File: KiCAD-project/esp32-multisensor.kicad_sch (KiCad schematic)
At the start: 21 parts, among them J1 USB_C_Receptacle_USB2.0, SW1 RST, SW3 BOOT, U1 ESP32-WROOM-E, U2 AMS1117-3.3, U3 TPD4E02B04DQA

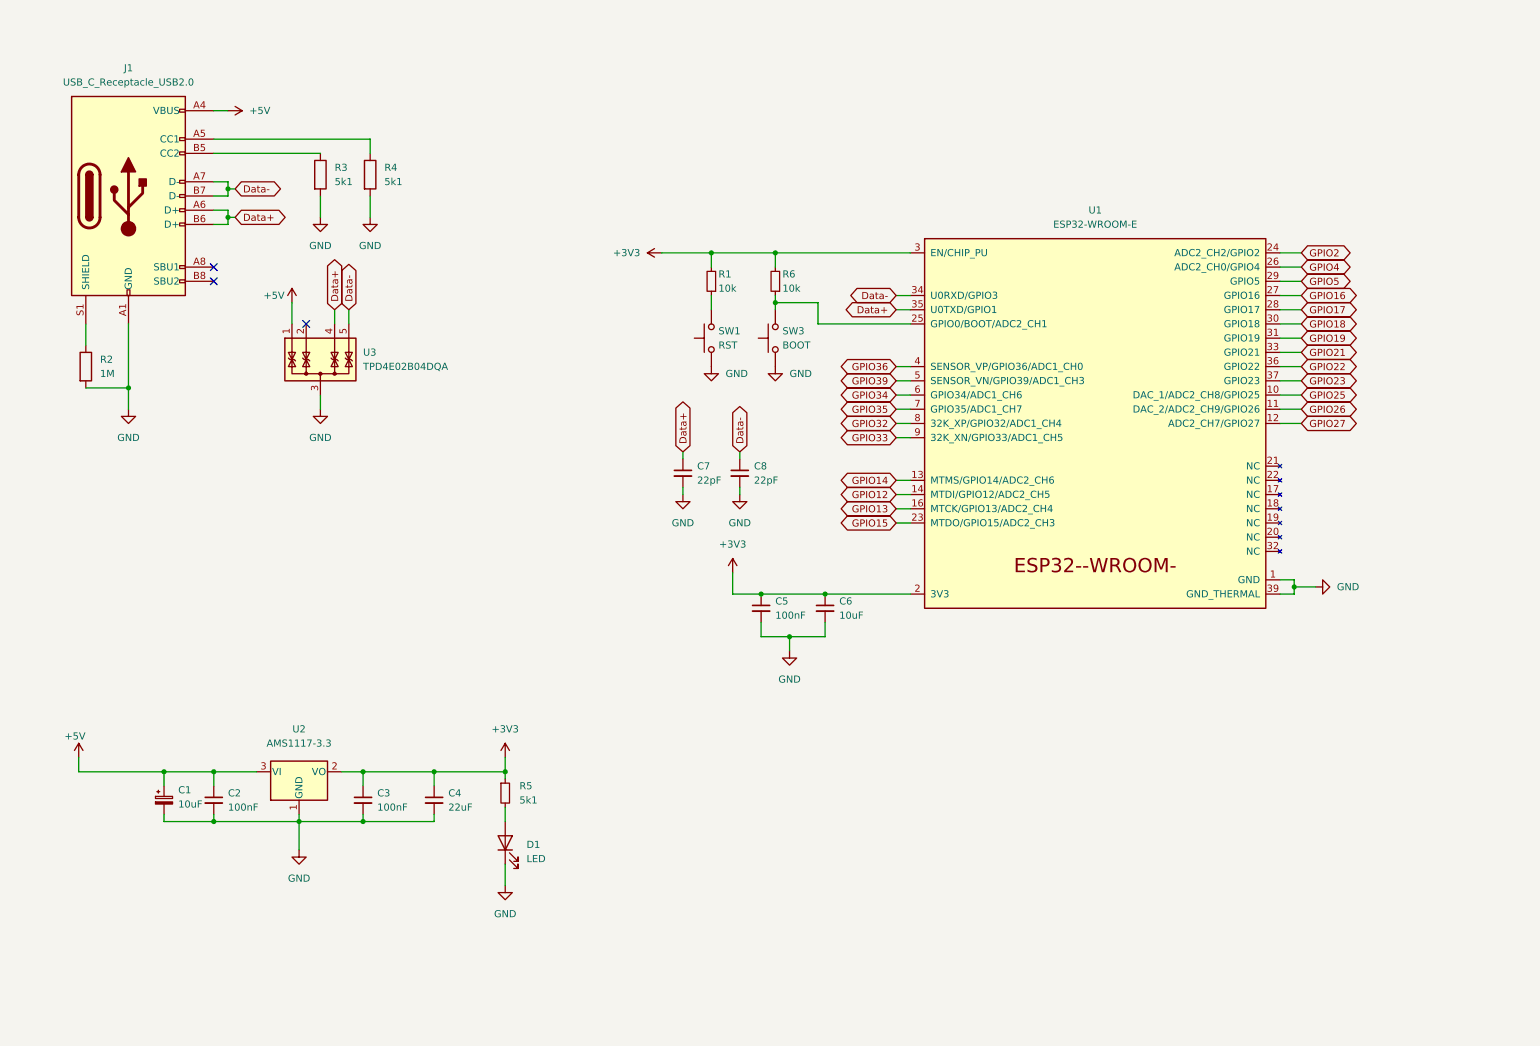
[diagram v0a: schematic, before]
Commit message: schematic created + base pcb
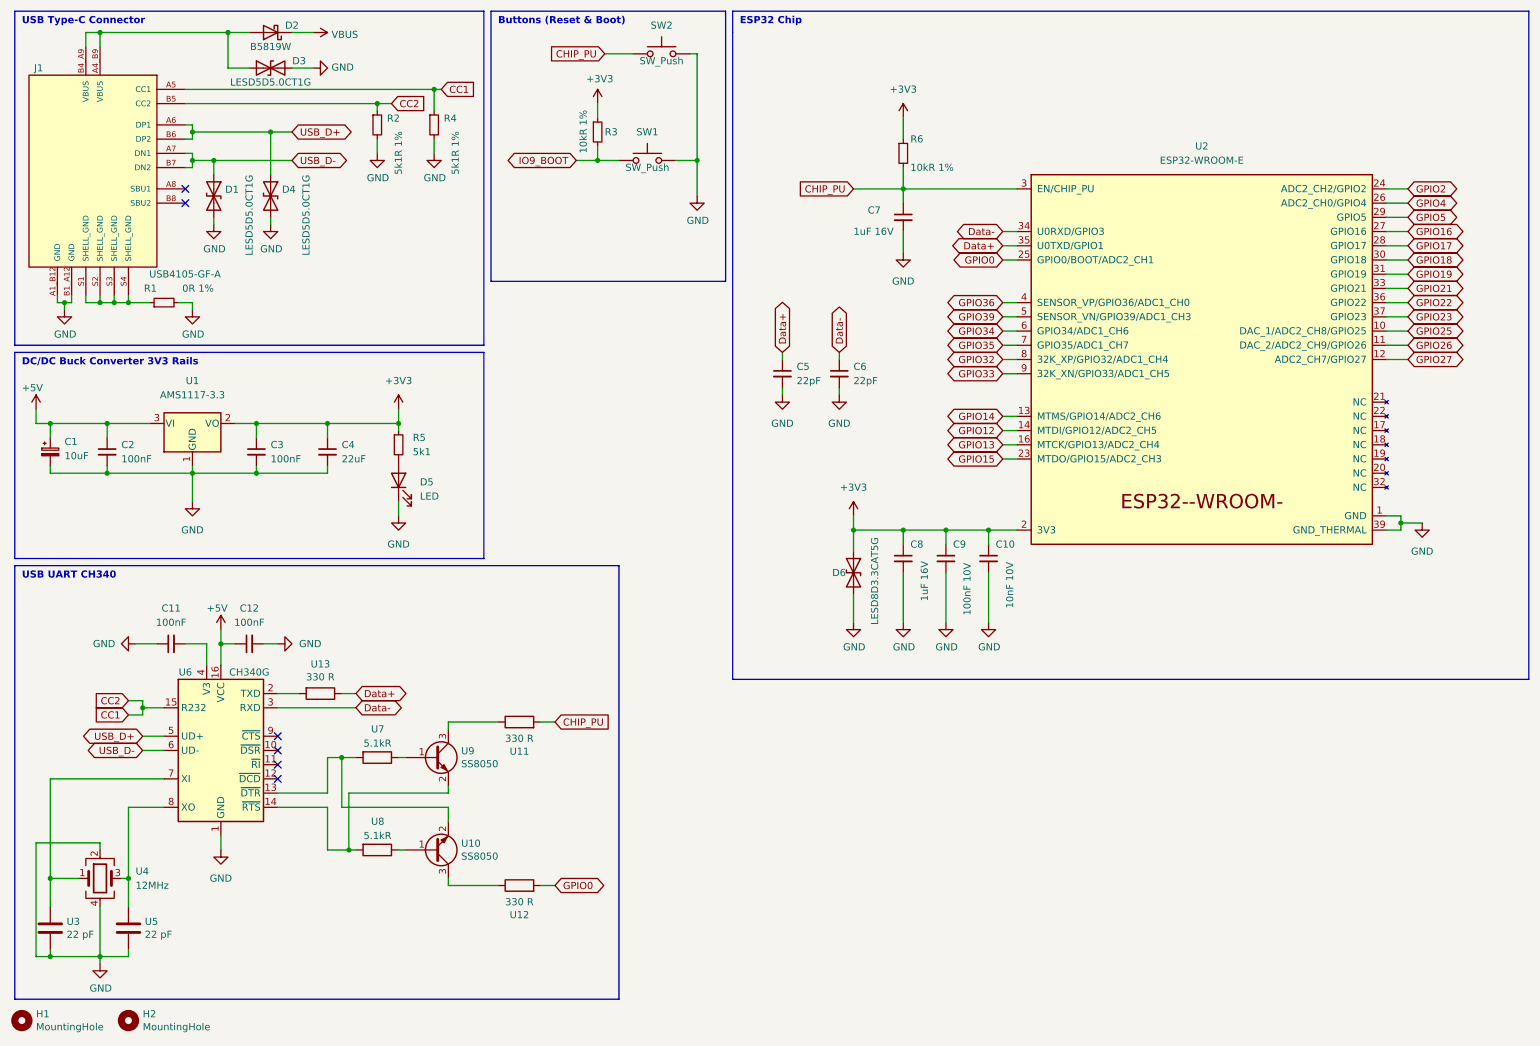
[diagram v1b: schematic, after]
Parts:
- removed C5: 100nF, symbol Device:C_Small
- removed C6: 10uF, symbol Device:C_Small
- removed J1: USB_C_Receptacle_USB2.0, Connector_USB:USB_C_Receptacle_HRO_TYPE-C-31-M-12, symbol Connector:USB_C_Receptacle_USB2.0
- removed R2: 1M, Resistor_SMD:R_0805_2012Metric_Pad1.20x1.40mm_HandSolder, symbol Device:R
- removed R3, R4: 5k1, Resistor_SMD:R_0805_2012Metric_Pad1.20x1.40mm_HandSolder, symbol Device:R
- removed SW3: BOOT, Button_Switch_SMD:SW_Push_1P1T_NO_CK_KMR2, symbol Switch:SW_Push
- removed U3: TPD4E02B04DQA, Package_SON:USON-10_2.5x1.0mm_P0.5mm, symbol Power_Protection:TPD4E02B04DQA
- added C10: 10nF 10V, Capacitor_THT:CP_Radial_D5.0mm_P2.50mm, symbol Device:C_Small
- added C11, C12: 100nF, Capacitor_THT:CP_Radial_D5.0mm_P2.50mm, symbol Device:C_Small
- added C7, C8: 1uF 16V, Capacitor_THT:CP_Radial_D5.0mm_P2.50mm, symbol Device:C_Small
- added C9: 100nF 10V, Capacitor_THT:CP_Radial_D5.0mm_P2.50mm, symbol Device:C_Small
- added D1, D4: LESD5D5.0CT1G, Diode_SMD:D_SOD-123, symbol Device:D_TVS
- added D2: B5819W, Diode_THT:D_A-405_P10.16mm_Horizontal, symbol Device:D_Schottky
- added D3: LESD5D5.0CT1G, Diode_SMD:D_SOD-923, symbol Device:D_TVS
- added D6: LESD8D3.3CAT5G, Rust_Board:SOD-882, symbol Device:D_TVS
- added H1, H2: MountingHole, ToolingHole:ToolingHole_JLCSMT, symbol Mechanical:MountingHole
- added J1: USB4105-GF-A, esp32_multisensor:GCT_USB4105-GF-A, symbol Rust_Board:USB4105-GF-A
- added R2, R4: 5k1R 1%, Resistor_THT:R_Axial_DIN0207_L6.3mm_D2.5mm_P10.16mm_Horizontal, symbol Device:R_Small
- added R3: 10kR 1%, Resistor_THT:R_Axial_DIN0207_L6.3mm_D2.5mm_P10.16mm_Horizontal, symbol Device:R_Small
- added SW2: SW_Push, esp32_multisensor:SW_147873-2, symbol Switch:SW_Push
- added U10, U9: SS8050, Package_TO_SOT_SMD:SOT-23, symbol Transistor_BJT:MMBT3904
- added U11, U12, U13: 330 R, Resistor_SMD:R_0402_1005Metric, symbol Device:R
- added U3, U5: 22 pF, Capacitor_SMD:C_0402_1005Metric, symbol Device:C
- added U4: 12MHz, Crystal:Crystal_SMD_3225-4Pin_3.2x2.5mm, symbol Device:Crystal_GND24
- added U6: CH340G, Package_SO:SOIC-16_3.9x9.9mm_P1.27mm, symbol Interface_USB:CH340G
- added U7, U8: 5.1kR, Resistor_SMD:R_0402_1005Metric, symbol Device:R
- C1: footprint (none) -> Capacitor_THT:CP_Radial_Tantal_D4.5mm_P2.50mm
- C2, C3, C4: footprint (none) -> Capacitor_THT:CP_Radial_D5.0mm_P2.50mm
- C5: renamed from C7; footprint (none) -> Capacitor_THT:CP_Radial_D5.0mm_P2.50mm
- C6: renamed from C8; footprint (none) -> Capacitor_THT:CP_Radial_D5.0mm_P2.50mm
- D5: renamed from D1; footprint (none) -> LED_SMD:LED_0805_2012Metric_Pad1.15x1.40mm_HandSolder
- R1: value 10k -> 0R 1%; footprint Resistor_SMD:R_0805_2012Metric_Pad1.20x1.40mm_HandSolder -> Resistor_THT:R_Axial_DIN0207_L6.3mm_D2.5mm_P10.16mm_Horizontal; FARNELL (none) -> 2329957
- R5: footprint Resistor_SMD:R_0805_2012Metric_Pad1.20x1.40mm_HandSolder -> Resistor_THT:R_Axial_DIN0207_L6.3mm_D2.5mm_P10.16mm_Horizontal
- R6: value 10k -> 10kR 1%; footprint Resistor_SMD:R_0805_2012Metric_Pad1.20x1.40mm_HandSolder -> Resistor_THT:R_Axial_DIN0207_L6.3mm_D2.5mm_P10.16mm_Horizontal; FARNELL (none) -> 2329855
- SW1: value RST -> SW_Push; footprint Button_Switch_SMD:SW_Push_1P1T_NO_CK_KMR2 -> esp32_multisensor:SW_147873-2; LCSC (none) -> C116501
- renumbered U2 to U1, U1 to U2
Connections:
- net +3V3: now also R6.1, C10.1, C8.1, C9.1, D6.1 (A1), R3.1; no longer R1.2, R6.2, U2.3 (EN/CHIP_PU)
- net +5V: now also C12.1, U6.16 (VCC)
- net Data+: now also U13.1
- net Data-: now also U6.3 (RXD)
- net GND: now also R1.2, SW1.2, C10.2, C11.1, C12.2, C7.2, C8.2, C9.2, D1.2 (A2), D3.2 (A2), D4.2 (A2), D6.2 (A2), J1.A1_B12 (GND), J1.B1_A12 (GND), R2.2, R4.2, SW2.2, U3.2, U4.2, U4.4, U5.2, U6.1 (GND); no longer SW1.1
- net GPIO0: now reaches U2.25 (GPIO0/BOOT/ADC2_CH1)
- net GPIO0: now also U12.2; no longer R6.1
- net at R1.1: now also J1.S1 (SHELL_GND), J1.S2 (SHELL_GND), J1.S3 (SHELL_GND), J1.S4 (SHELL_GND); no longer SW1.2
- new net: U11.1, U9.3 (C)
- new net: U13.2, U6.2 (TXD)
- new net: D2.2 (A), D3.1 (A1), J1.A4_B9 (VBUS), J1.B4_A9 (VBUS)
- new net: U3.1, U4.1, U6.7 (XI)
- new net: U4.3, U5.1, U6.8 (XO)
- new net: U10.1 (B), U8.1
- new net: U10.2 (E), U6.13 (~{DTR}), U7.2
- new net: U10.3 (C), U12.1
- new net: C11.2, U6.4 (V3)
- new net: U6.14 (~{RTS}), U8.2, U9.2 (E)
- new net: U7.1, U9.1 (B)
- new net CC1: J1.A5 (CC1), J1.B5 (CC2), R2.1, R4.1, U6.15 (R232)
- new net CHIP_PU: C7.1, R6.2, SW2.1, U11.2, U2.3 (EN/CHIP_PU)
- new net IO9_BOOT: R3.2, SW1.1
- new net USB_D+: D4.1 (A1), J1.A6 (DP1), J1.B6 (DP2), U6.5 (UD+)
- new net USB_D-: D1.1 (A1), J1.A7 (DN1), J1.B7 (DN2), U6.6 (UD-)
- new net VBUS: D2.1 (K)
- no-connect marks 3 -> 6
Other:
- note added: "Buttons (Reset & Boot)"
- note added: "DC/DC Buck Converter 3V3 Rails"
- note added: "ESP32 Chip"
- note added: "USB Type-C Connector"
- note added: "USB UART CH340"
- title: (none) -> ESP32 MultiSensor
- moved on the sheet: C1, C2, C3, C4, C5, C6, D5, R5, U1, U2
